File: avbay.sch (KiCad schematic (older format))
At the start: 2 parts

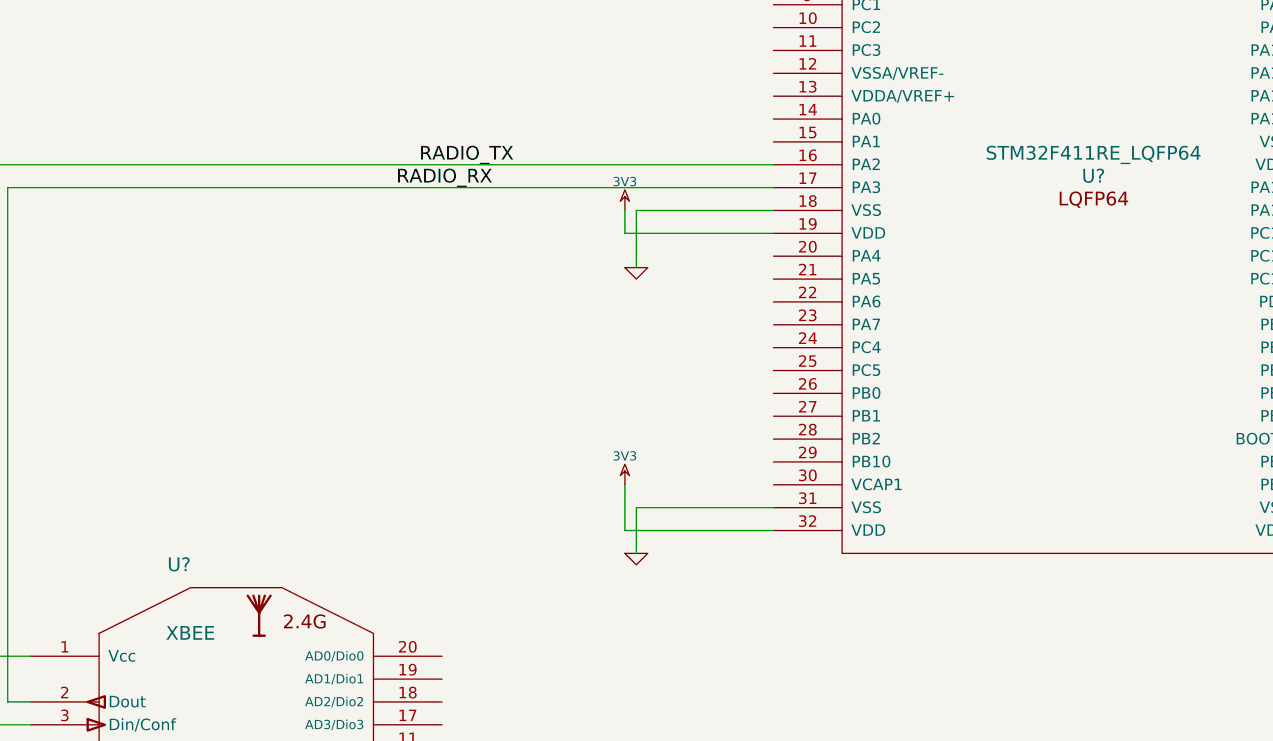
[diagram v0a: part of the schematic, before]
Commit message: Associated footprints
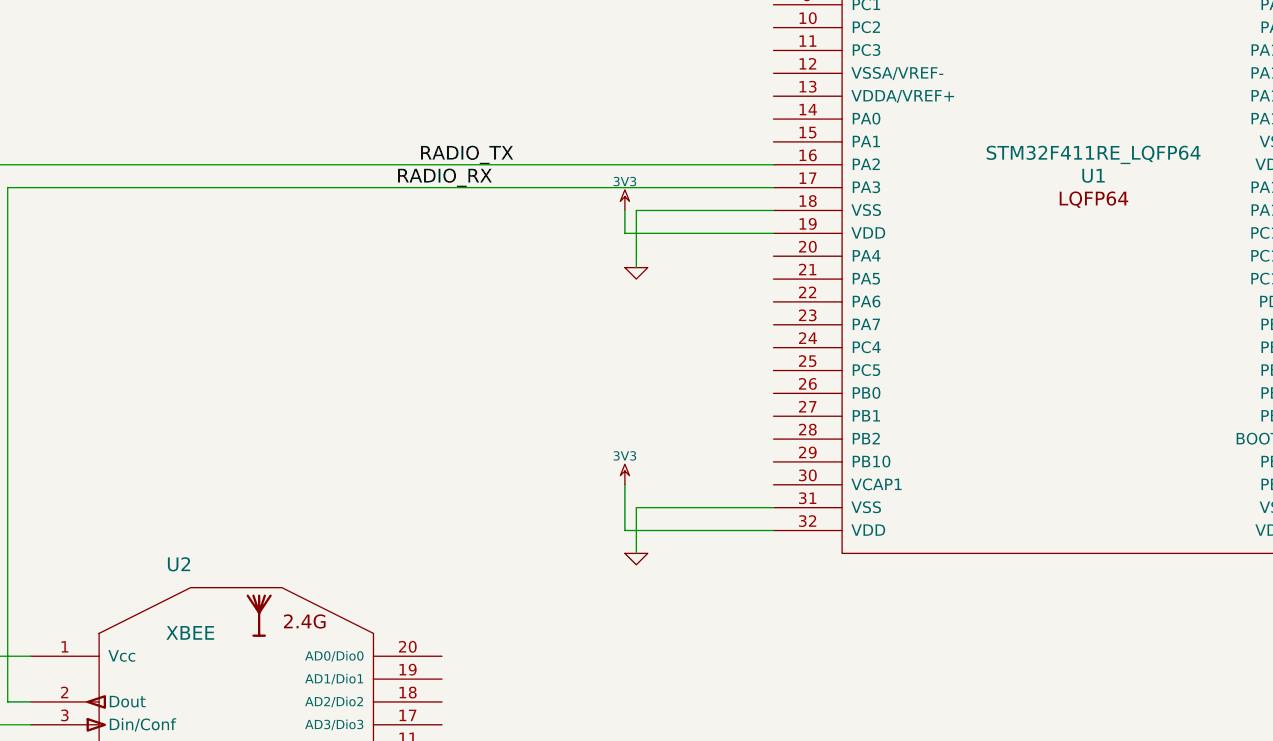
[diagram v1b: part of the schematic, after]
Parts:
- gave numbers to parts that had none: 2
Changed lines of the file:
@@
 $EndDescr
 $Comp
-L STM32F411RE_LQFP64 U?
+L STM32F411RE_LQFP64 U1
 U 1 1 542CD87C
 P 5850 3450
-F 0 "U?" H 5850 3450 60  0000 C CNN
+F 0 "U1" H 5850 3450 60  0000 C CNN
 F 1 "STM32F411RE_LQFP64" H 5850 3550 60  0000 C CNN
 F 2 "" H 5850 3600 60  0000 C CNN
@@
 $EndComp
 $Comp
-L XBEE U?
+L XBEE U2
 U 1 1 542CD8A3
 P 2100 6250
-F 0 "U?" H 1850 7350 60  0000 C CNN
+F 0 "U2" H 1850 7350 60  0000 C CNN
 F 1 "XBEE" H 1900 7050 60  0000 C CNN
 F 2 "" H 2100 6250 60  0000 C CNN
@@
 RADIO_RX
 $Comp
-L 3V3 #PWR?
+L 3V3 #PWR3
 U 1 1 542CDA8F
 P 3800 3600
-F 0 "#PWR?" H 3800 3700 40  0001 C CNN
+F 0 "#PWR3" H 3800 3700 40  0001 C CNN
 F 1 "3V3" H 3800 3725 40  0000 C CNN
 F 2 "" H 3800 3600 60  0000 C CNN
@@
 $EndComp
 $Comp
-L GND #PWR?
+L GND #PWR4
 U 1 1 542CDA9E
 P 3850 3850
-F 0 "#PWR?" H 3850 3850 30  0001 C CNN
+F 0 "#PWR4" H 3850 3850 30  0001 C CNN
 F 1 "GND" H 3850 3780 30  0001 C CNN
 F 2 "" H 3850 3850 60  0000 C CNN
@@
 $EndComp
 $Comp
-L 3V3 #PWR?
+L 3V3 #PWR9
 U 1 1 542CDAAB
 P 950 5350
-F 0 "#PWR?" H 950 5450 40  0001 C CNN
+F 0 "#PWR9" H 950 5450 40  0001 C CNN
 F 1 "3V3" H 950 5475 40  0000 C CNN
 F 2 "" H 950 5350 60  0000 C CNN
@@
 $EndComp
 $Comp
-L 3V3 #PWR?
+L 3V3 #PWR5
 U 1 1 542CDAB1
 P 3800 4800
-F 0 "#PWR?" H 3800 4900 40  0001 C CNN
+F 0 "#PWR5" H 3800 4900 40  0001 C CNN
 F 1 "3V3" H 3800 4925 40  0000 C CNN
 F 2 "" H 3800 4800 60  0000 C CNN
@@
 $EndComp
 $Comp
-L 3V3 #PWR?
+L 3V3 #PWR6
 U 1 1 542CDAB7
 P 7450 4850
-F 0 "#PWR?" H 7450 4950 40  0001 C CNN
+F 0 "#PWR6" H 7450 4950 40  0001 C CNN
 F 1 "3V3" H 7450 4975 40  0000 C CNN
 F 2 "" H 7450 4850 60  0000 C CNN
@@
 $EndComp
 $Comp
-L GND #PWR?
+L GND #PWR10
 U 1 1 542CDABD
 P 1150 6750
-F 0 "#PWR?" H 1150 6750 30  0001 C CNN
+F 0 "#PWR10" H 1150 6750 30  0001 C CNN
 F 1 "GND" H 1150 6680 30  0001 C CNN
 F 2 "" H 1150 6750 60  0000 C CNN
@@
 $EndComp
 $Comp
-L GND #PWR?
+L GND #PWR7
 U 1 1 542CDAC3
 P 3850 5100
-F 0 "#PWR?" H 3850 5100 30  0001 C CNN
+F 0 "#PWR7" H 3850 5100 30  0001 C CNN
 F 1 "GND" H 3850 5030 30  0001 C CNN
 F 2 "" H 3850 5100 60  0000 C CNN
@@
 $EndComp
 $Comp
-L GND #PWR?
+L GND #PWR8
 U 1 1 542CDAC9
 P 7400 5100
-F 0 "#PWR?" H 7400 5100 30  0001 C CNN
+F 0 "#PWR8" H 7400 5100 30  0001 C CNN
 F 1 "GND" H 7400 5030 30  0001 C CNN
 F 2 "" H 7400 5100 60  0000 C CNN
 F 3 "" H 7400 5100 60  0000 C CNN
 	1    7400 5100
+	1    0    0    -1
+$EndComp
+$Comp
+L 3V3 #PWR1
+U 1 1 542CDC4D
+P 7450 3250
+F 0 "#PWR1" H 7450 3350 40  0001 C CNN
+F 1 "3V3" H 7450 3375 40  0000 C CNN
+F 2 "" H 7450 3250 60  0000 C CNN
+F 3 "" H 7450 3250 60  0000 C CNN
+	1    7450 3250
+	1    0    0    -1
+$EndComp
+$Comp
+L GND #PWR2
+U 1 1 542CDC53
+P 7350 3450
+F 0 "#PWR2" H 7350 3450 30  0001 C CNN
+F 1 "GND" H 7350 3380 30  0001 C CNN
+F 2 "" H 7350 3450 60  0000 C CNN
+F 3 "" H 7350 3450 60  0000 C CNN
+	1    7350 3450
 	1    0    0    -1
 $EndComp
@@
 Wire Wire Line
 	1150 6650 1150 6750
-$Comp
-L 3V3 #PWR?
-U 1 1 542CDC4D
-P 7450 3250
-F 0 "#PWR?" H 7450 3350 40  0001 C CNN
-F 1 "3V3" H 7450 3375 40  0000 C CNN
-F 2 "" H 7450 3250 60  0000 C CNN
-F 3 "" H 7450 3250 60  0000 C CNN
-	1    7450 3250
-	1    0    0    -1
-$EndComp
-$Comp
-L GND #PWR?
-U 1 1 542CDC53
-P 7350 3450
-F 0 "#PWR?" H 7350 3450 30  0001 C CNN
-F 1 "GND" H 7350 3380 30  0001 C CNN
-F 2 "" H 7350 3450 60  0000 C CNN
-F 3 "" H 7350 3450 60  0000 C CNN
-	1    7350 3450
-	1    0    0    -1
-$EndComp
 Wire Wire Line
 	7050 3300 7350 3300

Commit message: Prototype made
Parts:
- removed U1: STM32F411RE_LQFP64, symbol STM32F411RE_LQFP64
- added JP1, JP2: JUMPER3, ~, symbol JUMPER3
- added P1, P3, P4: CONN_2, symbol CONN_2
- added P2: CONN_6, symbol CONN_6
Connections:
- net 3V3: now also P2.1
- net GND: now also P2.3
- net RADIO_RX renamed XBEE_TX
- net XBEE_TX: now also JP2.3
- net RADIO_TX renamed XBEE_RX
- net XBEE_RX: now also JP1.3
- new net MCU/JTCK-SWCLK: P2.2
- new net MCU/JTDO-SWO: P2.6
- new net MCU/JTMS-SWDIO: P2.4
- new net MCU/NRST: P2.5
- new net MCU/RADIO_RX: JP2.2
- new net MCU/RADIO_TX: JP1.2
- new net MCU/USART_RX: P3.2 (PM)
- new net MCU/USART_TX: P3.1 (P1)
- new net MCU/VDDA: P1.1 (P1)
- new net MCU/VSSA: P1.2 (PM)
- new net OVERRIDE_RX: JP2.1, P4.2 (PM)
- new net OVERRIDE_TX: JP1.1, P4.1 (P1)
- no-connect marks 0 -> 16

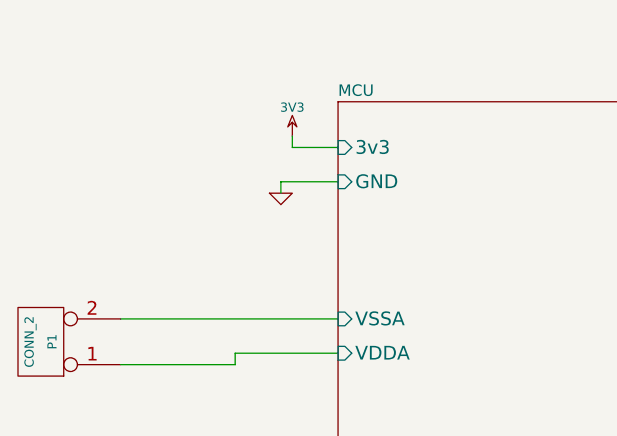
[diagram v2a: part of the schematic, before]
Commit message: Placed and routed basic PCB
Gonna end up throwing the whole thing out.

Needs to have GPIO headers added because reasons.
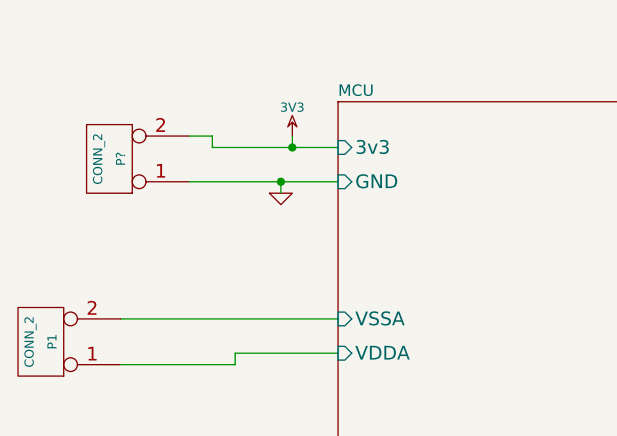
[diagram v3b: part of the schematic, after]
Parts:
- added P?: CONN_2, symbol CONN_2
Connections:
- net 3V3: now also P?.2 (PM)
- net GND: now also P?.1 (P1)
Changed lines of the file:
@@
 	7600 2650 8050 2650
 Wire Wire Line
-	4900 2800 4700 2800
-Wire Wire Line
-	4650 2950 4900 2950
+	4350 2800 4900 2800
+Wire Wire Line
+	4250 2950 4900 2950
 Wire Wire Line
 	8050 2550 7850 2550
@@
 Text Label 8300 4300 0    60   ~ 0
 OVERRIDE_RX
+$Comp
+L CONN_2 P?
+U 1 1 5430FC07
+P 3900 2850
+F 0 "P?" V 3850 2850 40  0000 C CNN
+F 1 "CONN_2" V 3950 2850 40  0000 C CNN
+F 2 "" H 3900 2850 60  0000 C CNN
+F 3 "" H 3900 2850 60  0000 C CNN
+	1    3900 2850
+	-1   0    0    1
+$EndComp
+Connection ~ 4650 2950
+Wire Wire Line
+	4350 2800 4350 2750
+Wire Wire Line
+	4350 2750 4250 2750
+Connection ~ 4700 2800
 $EndSCHEMATC

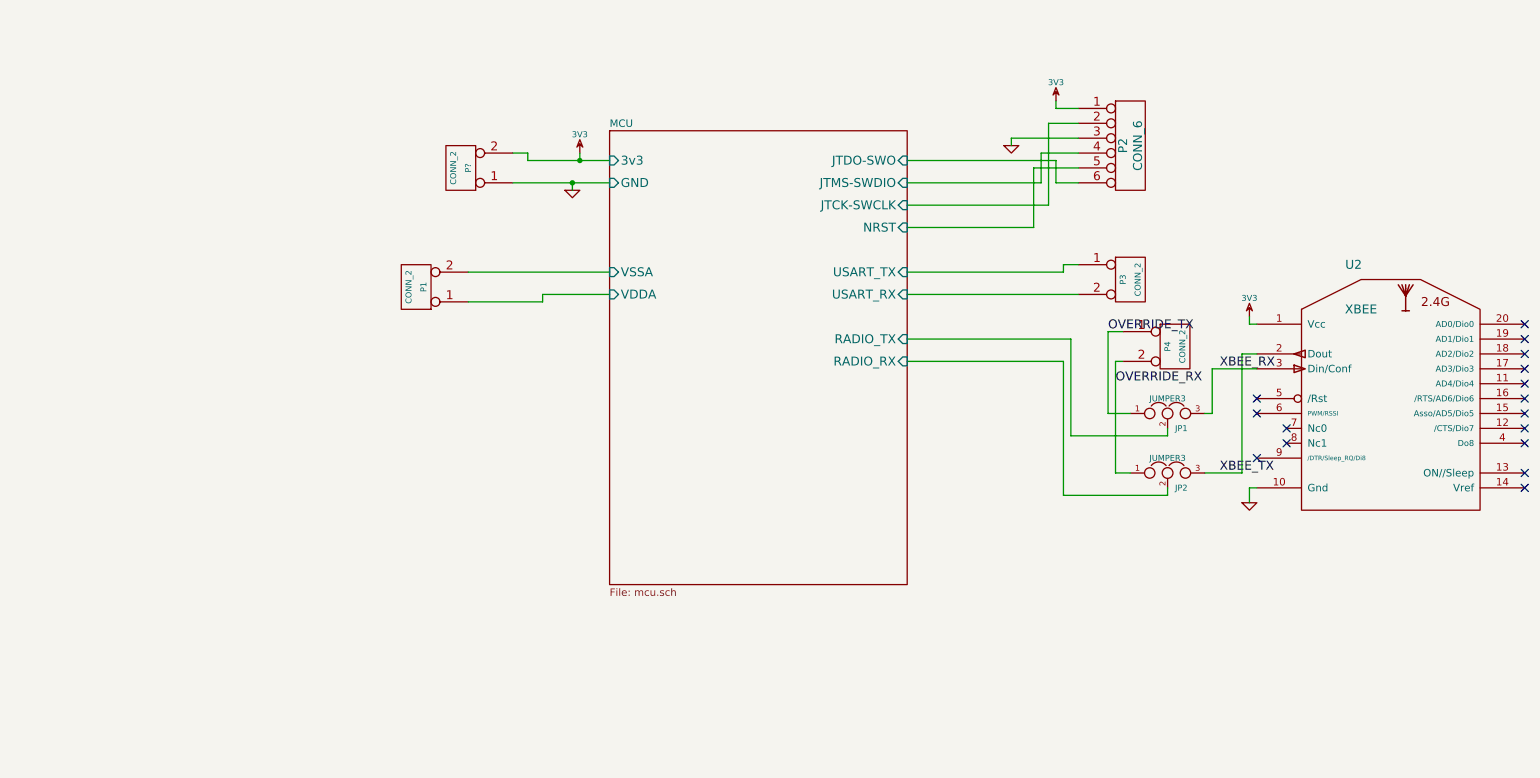
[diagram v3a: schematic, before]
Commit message: Added voltage regulators
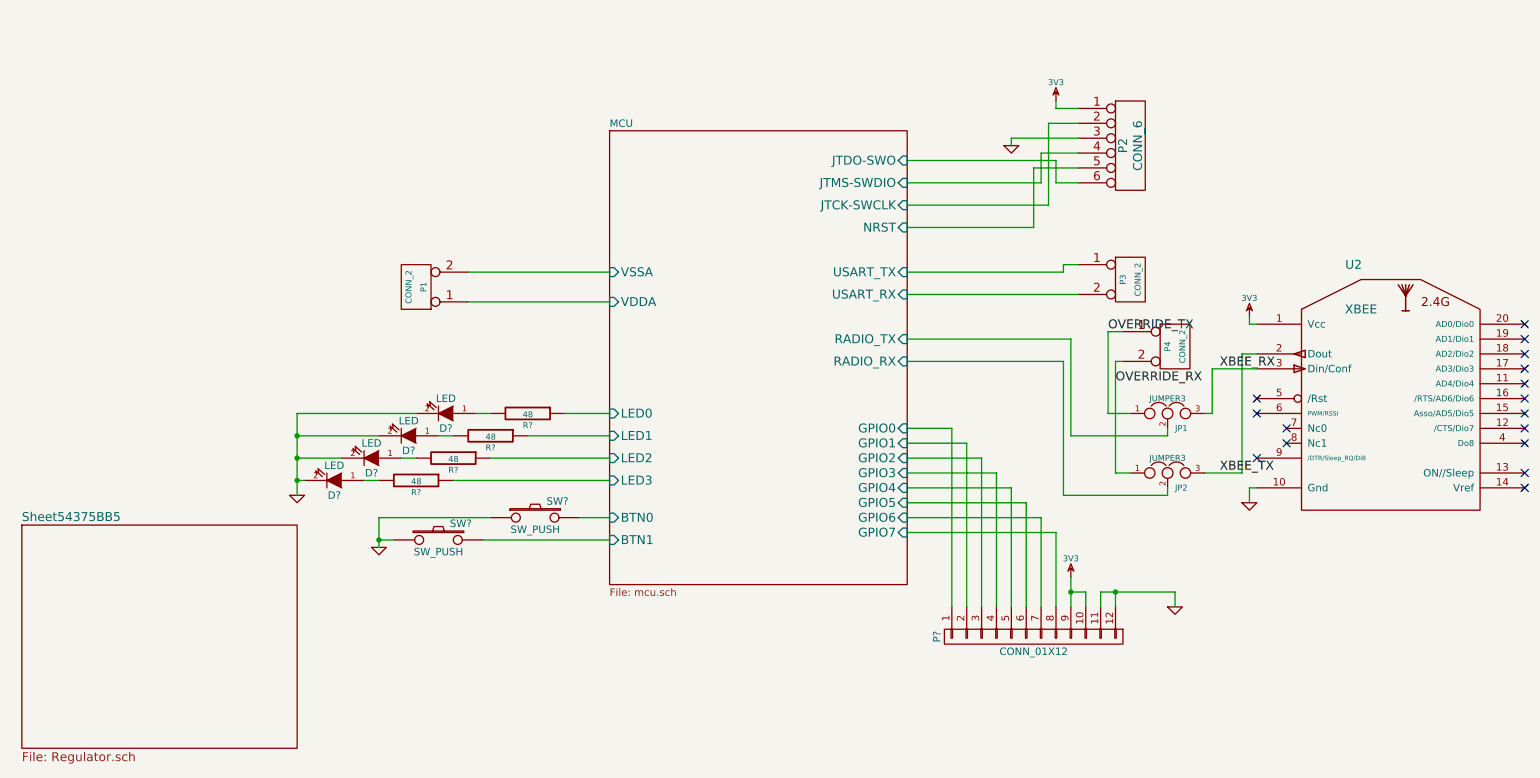
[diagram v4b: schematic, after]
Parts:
- removed P?: CONN_2, symbol CONN_2
- added D? (x4): LED, symbol LED
- added P?: CONN_01X12, symbol CONN_01X12
- added R? (x4): 48, symbol R
- added SW? (x2): SW_PUSH, symbol SW_PUSH
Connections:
- net 3V3: now also P?.10 (P10), P?.9 (P9)
- net GND: now also D?.2 (K), D?.2 (K), D?.2 (K), D?.2 (K), P?.11 (P11), P?.12 (P12), SW?.1, SW?.1
- new net: D?.1 (A), R?.2 (x4)
- new net MCU/BTN0: SW?.2
- new net MCU/BTN1: SW?.2
- new net MCU/GPIO0: P?.1 (P1)
- new net MCU/GPIO1: P?.2 (P2)
- new net MCU/GPIO2: P?.3 (P3)
- new net MCU/GPIO3: P?.4 (P4)
- new net MCU/GPIO4: P?.5 (P5)
- new net MCU/GPIO5: P?.6 (P6)
- new net MCU/GPIO6: P?.7 (P7)
- new net MCU/GPIO7: P?.8 (P8)
- new net MCU/LED0: R?.1
- new net MCU/LED1: R?.1
- new net MCU/LED2: R?.1
- new net MCU/LED3: R?.1

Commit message: Began layout of board
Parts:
- added BT1: BATTERY, ~, symbol BATTERY
- gave numbers to parts that had none: 11
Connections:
- net GND: now also BT1.2 (-)
- new net Sheet54375BB5/Vbatt: BT1.1 (+)
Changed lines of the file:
@@
 LIBS:xbee
 LIBS:avbay-cache
-EELAYER 25 0
+EELAYER 27 0
 EELAYER END
 $Descr A4 11693 8268
@@
 Sheet 1 3
 Title ""
-Date "5 oct 2014"
+Date "20 oct 2014"
 Rev ""
 Comp ""
@@
 $EndComp
 $Comp
-L GND #PWR4
+L GND #PWR01
 U 1 1 5430FA44
 P 9200 5100
-F 0 "#PWR4" H 9200 5100 30  0001 C CNN
+F 0 "#PWR01" H 9200 5100 30  0001 C CNN
 F 1 "GND" H 9200 5030 30  0001 C CNN
 F 2 "" H 9200 5100 60  0000 C CNN
@@
 $EndComp
 $Comp
-L 3V3 #PWR3
+L 3V3 #PWR02
 U 1 1 5430FA53
 P 9200 3850
-F 0 "#PWR3" H 9200 3950 40  0001 C CNN
+F 0 "#PWR02" H 9200 3950 40  0001 C CNN
 F 1 "3V3" H 9200 3975 40  0000 C CNN
 F 2 "" H 9200 3850 60  0000 C CNN
@@
 	3950 3750 4900 3750
 $Comp
-L 3V3 #PWR2
+L 3V3 #PWR03
 U 1 1 5430FF93
 P 7900 2400
-F 0 "#PWR2" H 7900 2500 40  0001 C CNN
+F 0 "#PWR03" H 7900 2500 40  0001 C CNN
 F 1 "3V3" H 7900 2525 40  0000 C CNN
 F 2 "" H 7900 2400 60  0000 C CNN
@@
 $EndComp
 $Comp
-L GND #PWR1
+L GND #PWR04
 U 1 1 5430FF99
 P 7600 2700
-F 0 "#PWR1" H 7600 2700 30  0001 C CNN
+F 0 "#PWR04" H 7600 2700 30  0001 C CNN
 F 1 "GND" H 7600 2630 30  0001 C CNN
 F 2 "" H 7600 2700 60  0000 C CNN
@@
 F0 "Sheet54375BB5" 60
 F1 "Regulator.sch" 60
+F2 "Vbatt" I R 2800 6300 60
 $EndSheet
 Wire Wire Line
@@
 	4900 4950 3850 4950
 $Comp
-L R R?
+L R R5
 U 1 1 5437A174
 P 4350 4500
-F 0 "R?" V 4430 4500 40  0000 C CNN
+F 0 "R5" V 4430 4500 40  0000 C CNN
 F 1 "48" V 4357 4501 40  0000 C CNN
 F 2 "" V 4280 4500 30  0000 C CNN
@@
 $EndComp
 $Comp
-L R R?
+L R R4
 U 1 1 5437A32D
 P 4100 4650
-F 0 "R?" V 4180 4650 40  0000 C CNN
+F 0 "R4" V 4180 4650 40  0000 C CNN
 F 1 "48" V 4107 4651 40  0000 C CNN
 F 2 "" V 4030 4650 30  0000 C CNN
@@
 $EndComp
 $Comp
-L R R?
+L R R3
 U 1 1 5437A376
 P 3850 4800
-F 0 "R?" V 3930 4800 40  0000 C CNN
+F 0 "R3" V 3930 4800 40  0000 C CNN
 F 1 "48" V 3857 4801 40  0000 C CNN
 F 2 "" V 3780 4800 30  0000 C CNN
@@
 $EndComp
 $Comp
-L R R?
+L R R2
 U 1 1 5437A3A4
 P 3600 4950
-F 0 "R?" V 3680 4950 40  0000 C CNN
+F 0 "R2" V 3680 4950 40  0000 C CNN
 F 1 "48" V 3607 4951 40  0000 C CNN
 F 2 "" V 3530 4950 30  0000 C CNN
@@
 $EndComp
 $Comp
-L LED D?
+L LED D4
 U 1 1 5437A448
 P 3800 4500
-F 0 "D?" H 3800 4600 50  0000 C CNN
+F 0 "D4" H 3800 4600 50  0000 C CNN
 F 1 "LED" H 3800 4400 50  0000 C CNN
 F 2 "" H 3800 4500 60  0000 C CNN
@@
 	3350 4950 3250 4950
 $Comp
-L LED D?
+L LED D3
 U 1 1 5437A650
 P 3550 4650
-F 0 "D?" H 3550 4750 50  0000 C CNN
+F 0 "D3" H 3550 4750 50  0000 C CNN
 F 1 "LED" H 3550 4550 50  0000 C CNN
 F 2 "" H 3550 4650 60  0000 C CNN
@@
 $EndComp
 $Comp
-L LED D?
+L LED D2
 U 1 1 5437A68B
 P 3300 4800
-F 0 "D?" H 3300 4900 50  0000 C CNN
+F 0 "D2" H 3300 4900 50  0000 C CNN
 F 1 "LED" H 3300 4700 50  0000 C CNN
 F 2 "" H 3300 4800 60  0000 C CNN
@@
 $EndComp
 $Comp
-L LED D?
+L LED D1
 U 1 1 5437A6BD
 P 3050 4950
-F 0 "D?" H 3050 5050 50  0000 C CNN
+F 0 "D1" H 3050 5050 50  0000 C CNN
 F 1 "LED" H 3050 4850 50  0000 C CNN
 F 2 "" H 3050 4950 60  0000 C CNN
@@
 $EndComp
 $Comp
-L GND #PWR?
+L GND #PWR05
 U 1 1 5437A755
 P 2800 5050
-F 0 "#PWR?" H 2800 5050 30  0001 C CNN
+F 0 "#PWR05" H 2800 5050 30  0001 C CNN
 F 1 "GND" H 2800 4980 30  0001 C CNN
 F 2 "" H 2800 5050 60  0000 C CNN
@@
 Connection ~ 2800 4650
 $Comp
-L SW_PUSH SW?
+L SW_PUSH SW3
 U 1 1 5437AA50
 P 4400 5200
-F 0 "SW?" H 4550 5310 50  0000 C CNN
+F 0 "SW3" H 4550 5310 50  0000 C CNN
 F 1 "SW_PUSH" H 4400 5120 50  0000 C CNN
 F 2 "" H 4400 5200 60  0000 C CNN
@@
 $EndComp
 $Comp
-L SW_PUSH SW?
+L SW_PUSH SW2
 U 1 1 5437AAF9
 P 3750 5350
-F 0 "SW?" H 3900 5460 50  0000 C CNN
+F 0 "SW2" H 3900 5460 50  0000 C CNN
 F 1 "SW_PUSH" H 3750 5270 50  0000 C CNN
 F 2 "" H 3750 5350 60  0000 C CNN
@@
 	3350 5200 3350 5400
 $Comp
-L GND #PWR?
+L GND #PWR06
 U 1 1 5437AD2F
 P 3350 5400
-F 0 "#PWR?" H 3350 5400 30  0001 C CNN
+F 0 "#PWR06" H 3350 5400 30  0001 C CNN
 F 1 "GND" H 3350 5330 30  0001 C CNN
 F 2 "" H 3350 5400 60  0000 C CNN
@@
 Connection ~ 3350 5350
 $Comp
-L CONN_01X12 P?
+L CONN_01X12 P6
 U 1 1 5437E79B
 P 7750 6000
-F 0 "P?" H 7750 6650 50  0000 C CNN
+F 0 "P6" H 7750 6650 50  0000 C CNN
 F 1 "CONN_01X12" V 7850 6000 50  0000 C CNN
 F 2 "" H 7750 6000 60  0000 C CNN
@@
 	7900 5300 7900 5800
 $Comp
-L GND #PWR?
+L GND #PWR07
 U 1 1 5437EF10
 P 8700 5800
-F 0 "#PWR?" H 8700 5800 30  0001 C CNN
+F 0 "#PWR07" H 8700 5800 30  0001 C CNN
 F 1 "GND" H 8700 5730 30  0001 C CNN
 F 2 "" H 8700 5800 60  0000 C CNN
@@
 $EndComp
 $Comp
-L 3V3 #PWR?
+L 3V3 #PWR08
 U 1 1 5437EF24
 P 8000 5600
-F 0 "#PWR?" H 8000 5700 40  0001 C CNN
+F 0 "#PWR08" H 8000 5700 40  0001 C CNN
 F 1 "3V3" H 8000 5725 40  0000 C CNN
 F 2 "" H 8000 5600 60  0000 C CNN
@@
 	8100 5700 8000 5700
 Connection ~ 8000 5700
+Wire Wire Line
+	2800 6300 3450 6300
+Wire Wire Line
+	4200 6550 3050 6550
+Wire Wire Line
+	3050 6550 3050 6700
+$Comp
+L GND #PWR09
+U 1 1 54449D6F
+P 3050 6700
+F 0 "#PWR09" H 3050 6700 30  0001 C CNN
+F 1 "GND" H 3050 6630 30  0001 C CNN
+F 2 "" H 3050 6700 60  0000 C CNN
+F 3 "" H 3050 6700 60  0000 C CNN
+	1    3050 6700
+	1    0    0    -1
+$EndComp
+$Comp
+L BATTERY BT1
+U 1 1 54449F40
+P 3750 6300
+F 0 "BT1" H 3750 6500 50  0000 C CNN
+F 1 "BATTERY" H 3750 6110 50  0000 C CNN
+F 2 "~" H 3750 6300 60  0000 C CNN
+F 3 "~" H 3750 6300 60  0000 C CNN
+	1    3750 6300
+	1    0    0    -1
+$EndComp
+Wire Wire Line
+	4200 6300 4200 6550
+Wire Wire Line
+	4050 6300 4200 6300
 $EndSCHEMATC
